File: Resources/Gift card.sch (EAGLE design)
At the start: 27 parts, among them J1 USBSMD, J2 LPC_SWD_PINPROG, Q1 IRLML6402, Q2 IRLML2502SOT23, U1 LPC11U24FBD48/301, U2 MMA8452Q, U3 NCP551SN33T1G, U4 NCP551SN50T1G, Y1 SMDCRYSTAL

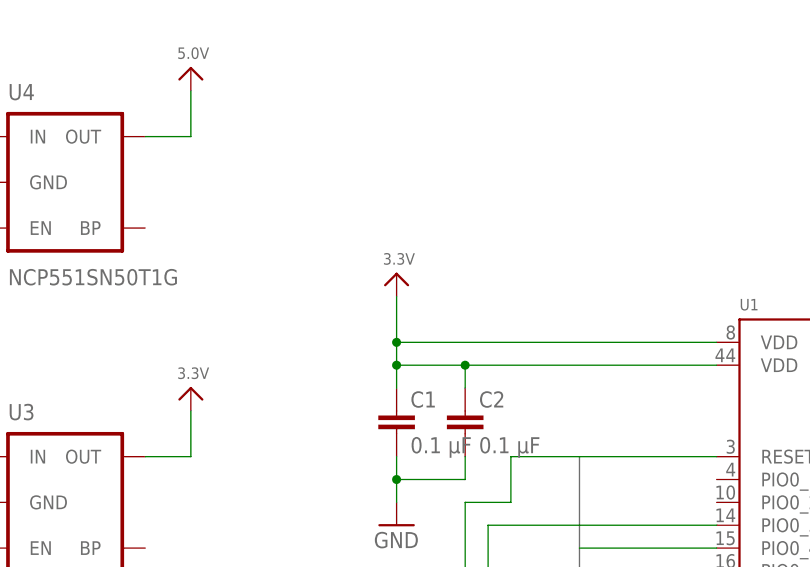
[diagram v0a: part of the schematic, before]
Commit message: Added drawable: hole; refactored abstraction error to #define
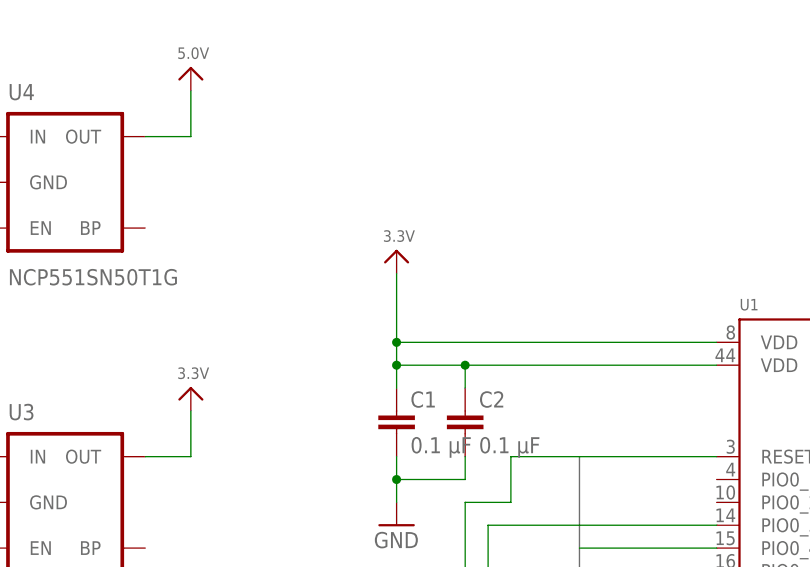
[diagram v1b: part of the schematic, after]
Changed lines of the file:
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@@
 <?xml version="1.0" encoding="utf-8"?>
 <!DOCTYPE eagle SYSTEM "eagle.dtd">
-<eagle version="6.4">
+<eagle version="6.5.0">
 <drawing>
 <settings>
@@
 <instance part="C8" gate="G$1" x="175.26" y="114.3" rot="R90"/>
 <instance part="GND5" gate="1" x="-78.74" y="45.72"/>
-<instance part="U$1" gate="G$1" x="-17.78" y="134.62"/>
+<instance part="U$1" gate="G$1" x="-17.78" y="137.16"/>
 <instance part="GND6" gate="1" x="129.54" y="116.84"/>
 <instance part="S1" gate="G$1" x="-78.74" y="91.44" rot="R90"/>
@@
 <pinref part="U$1" gate="G$1" pin="3.3V"/>
 <wire x1="-17.78" y1="124.46" x2="-17.78" y2="121.92" width="0.1524" layer="91"/>
-<wire x1="-17.78" y1="127" x2="-17.78" y2="132.08" width="0.1524" layer="91"/>
+<wire x1="-17.78" y1="127" x2="-17.78" y2="134.62" width="0.1524" layer="91"/>
 <junction x="-17.78" y="127"/>
 <pinref part="U1" gate="G$1" pin="VDD@2"/>
